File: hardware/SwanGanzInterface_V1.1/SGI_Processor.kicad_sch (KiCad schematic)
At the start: 31 parts, among them J2 Conn_01x08_Pin, SW2 MODE, SW3 ENTER, SW4 MODE, U4 XM0G3507QPTRQ1, U5 AdaFruit_1590, Y1 ABM8AIG-40.000MHZ-12-2Z-T3

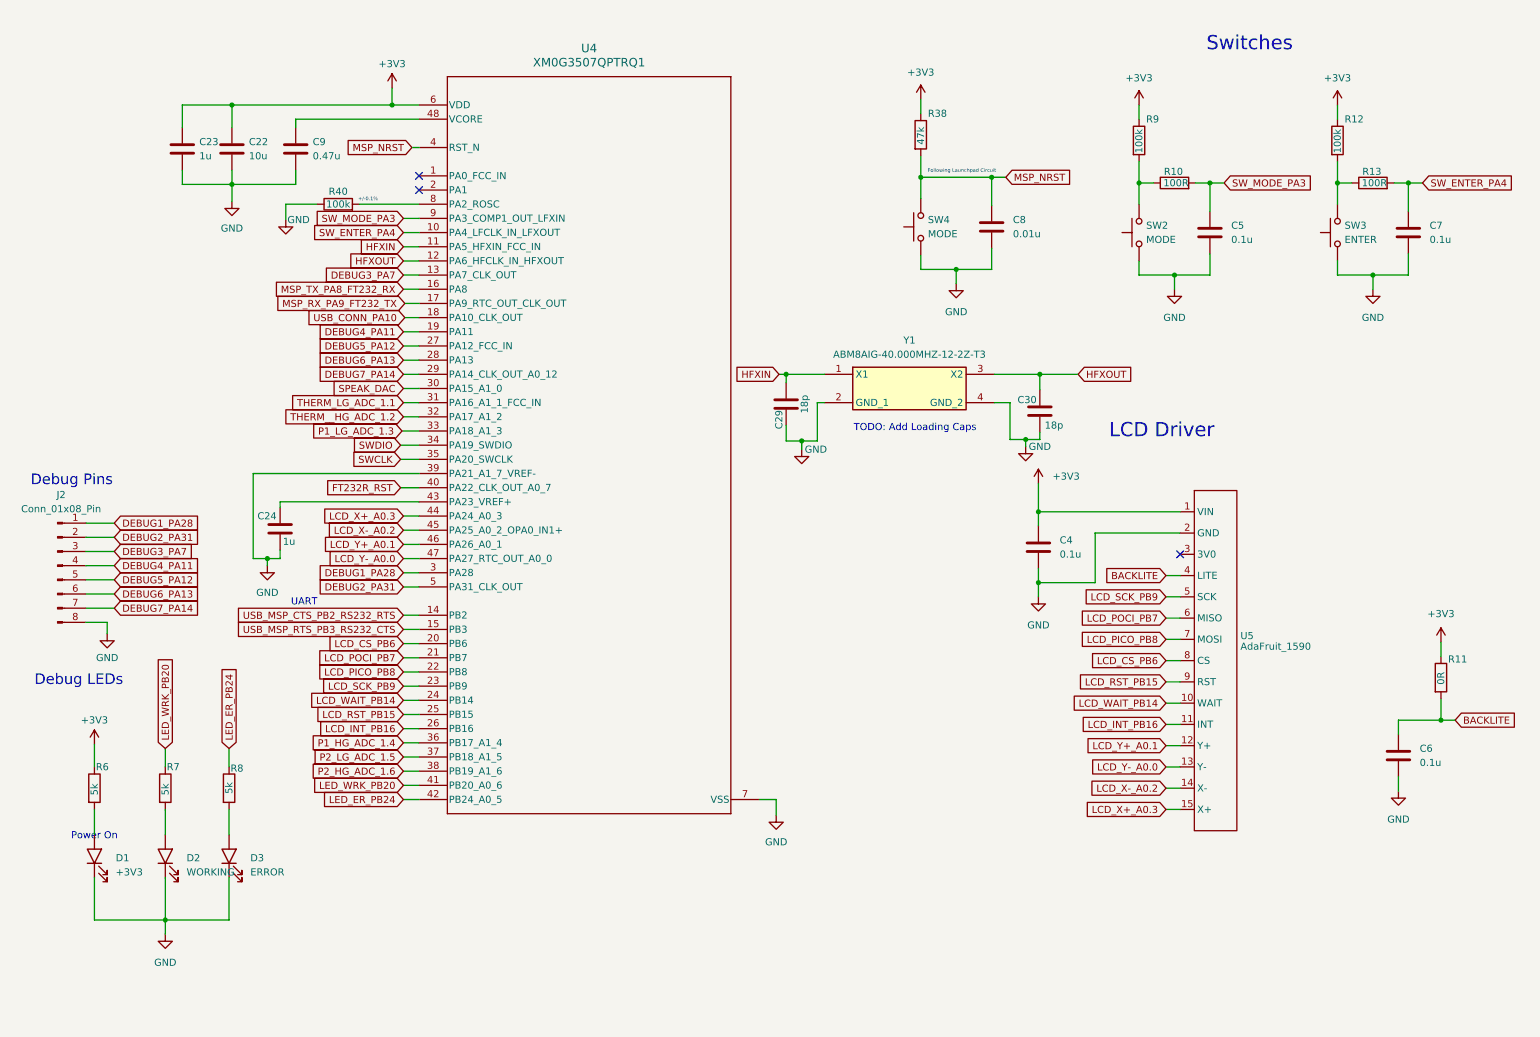
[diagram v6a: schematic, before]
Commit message: Started converting things to use touch screen chip
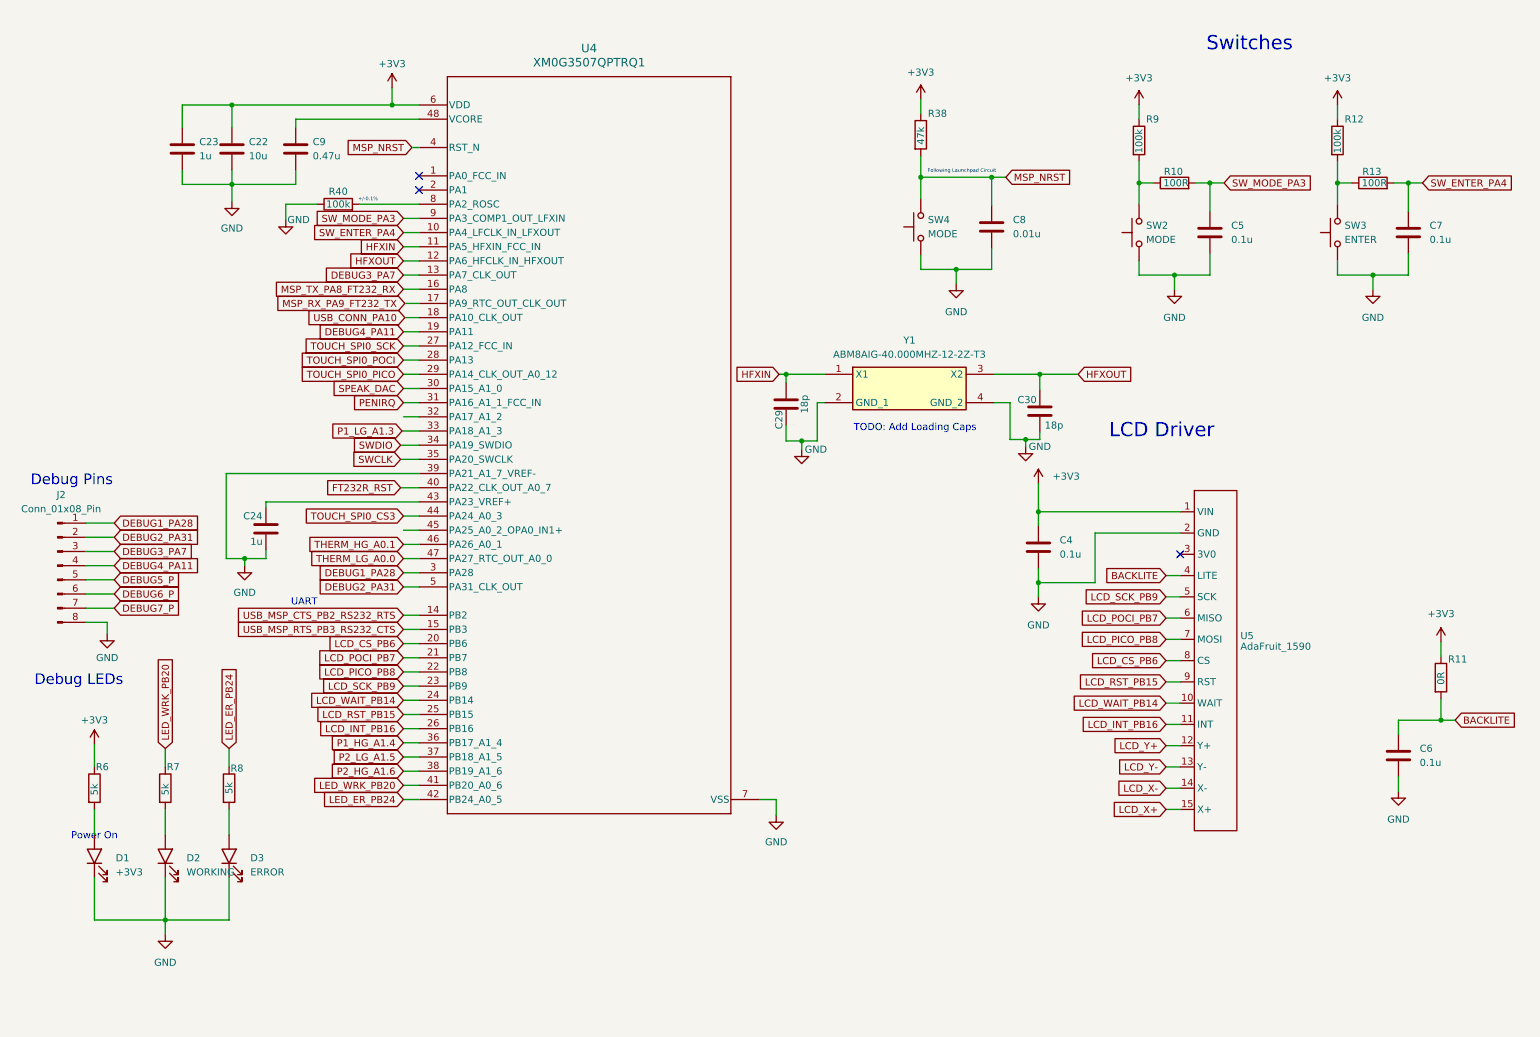
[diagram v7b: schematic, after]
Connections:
- net DEBUG5_PA12 renamed DEBUG5_P
- net DEBUG5_P: no longer U4.27 (PA12_FCC_IN)
- net DEBUG6_PA13 renamed DEBUG6_P
- net DEBUG6_P: no longer U4.28 (PA13)
- net DEBUG7_PA14 renamed DEBUG7_P
- net DEBUG7_P: no longer U4.29 (PA14_CLK_OUT_A0_12)
- net LCD_X+_A0.3 renamed LCD_X+
- net LCD_X+: no longer U4.44 (PA24_A0_3)
- net LCD_X-_A0.2: no longer names the net of U4.45 (PA25_A0_2_OPA0_IN1+)
- net LCD_X-_A0.2: no longer U5.14 (X-)
- net LCD_Y+_A0.1 renamed LCD_Y+
- net LCD_Y+: no longer U4.46 (PA26_A0_1)
- net LCD_Y-_A0.0 renamed LCD_Y-
- net LCD_Y-: no longer U4.47 (PA27_RTC_OUT_A0_0)
- net P1_HG_ADC_1.4 renamed P1_HG_A1.4
- net P1_LG_ADC_1.3 renamed P1_LG_A1.3
- net P2_HG_ADC_1.6 renamed P2_HG_A1.6
- net P2_LG_ADC_1.5 renamed P2_LG_A1.5
- net THERM_LG_ADC_1.1 renamed PENIRQ
- net THERM__HG_ADC_1.2: no longer names the net of U4.32 (PA17_A1_2)
- new net LCD_X-: U5.14 (X-)
- new net THERM_HG_A0.1: U4.46 (PA26_A0_1)
- new net THERM_LG_A0.0: U4.47 (PA27_RTC_OUT_A0_0)
- new net TOUCH_SPI0_CS3: U4.44 (PA24_A0_3)
- new net TOUCH_SPI0_PICO: U4.29 (PA14_CLK_OUT_A0_12)
- new net TOUCH_SPI0_POCI: U4.28 (PA13)
- new net TOUCH_SPI0_SCK: U4.27 (PA12_FCC_IN)
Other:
- moved on the sheet: C24

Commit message: Added lots, moving to 64 pin micro
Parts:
- removed C6: 0.1u, Capacitor_SMD:C_0603_1608Metric, symbol Device:C
- removed R11: 0R, Resistor_SMD:R_0603_1608Metric, symbol Device:R
- C29, C30: value 18p -> 30p
- R6, R7, R8: value 5k -> 2k
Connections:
- net BACKLITE is gone; now on net BACKLITE_PA25: U5.4 (LITE)
- net SPEAK_CD: now reaches U4.32 (PA17_A1_2)
- net BACKLITE_PA25: now reaches U4.45 (PA25_A0_2_OPA0_IN1+)
- net DEBUG5_P: no longer names the net of J2.5 (Pin_5)
- net DEBUG6_P: no longer names the net of J2.6 (Pin_6)
- net DEBUG7_P: no longer names the net of J2.7 (Pin_7)
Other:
- note added: "Add Button"
- note added: "C1, C2 = 2*CL – 2*Cstray CL = 18p Assume Cstray = ~3p C1, C2 = (2*18) - (2*3) = 36 - 6 C1,C2 = 30p"
- note removed: "TODO: Add Loading Caps"
- moved on the sheet: C4, U5
